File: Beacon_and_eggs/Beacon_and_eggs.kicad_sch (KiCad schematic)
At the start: 34 parts, among them SW1 Boot, SW2 Reset, U1 SA818V, U2 STM32F411CEUx, U3 ADXL343, U4 MIC2877-5.0YFT-TR, U5 LM3940ISX-3.3/NOPB, Y1 25MHz 18pF, Y2 32.768kHz 12.5pF

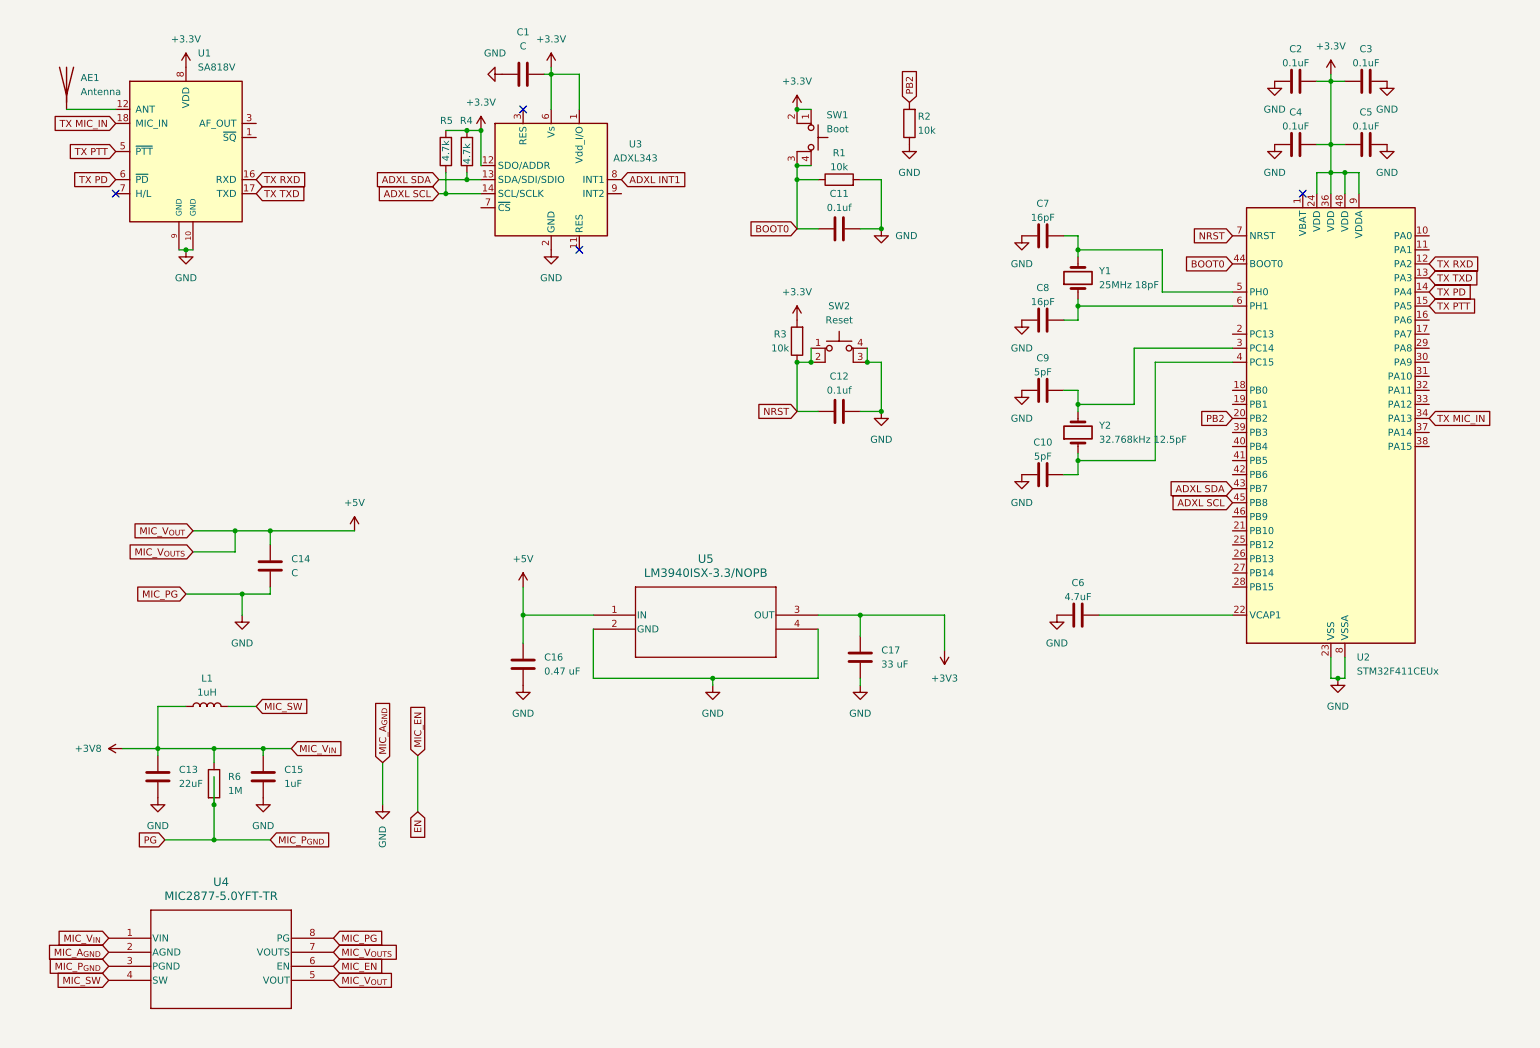
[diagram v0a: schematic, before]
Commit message: Reformatted Schematic Layout
cool beans
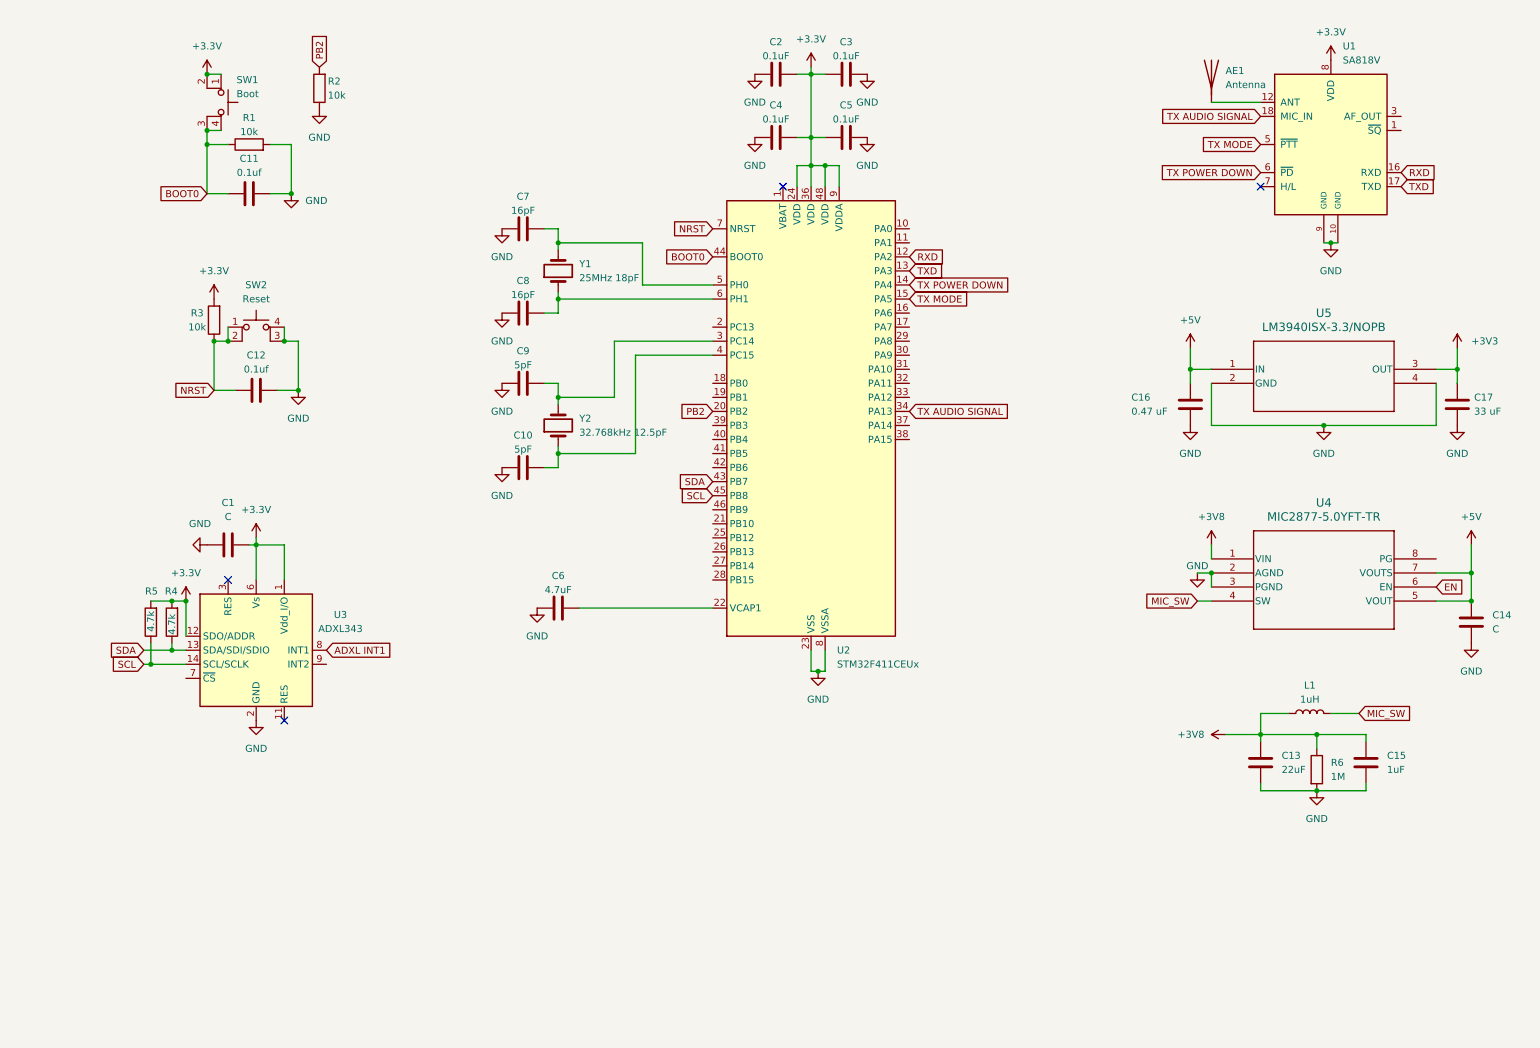
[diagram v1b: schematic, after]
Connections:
- net MIC_P_{GND} is gone; now on net GND: R6.2, U4.3 (PGND)
- net +5V: now also C14.2; no longer C14.1
- net GND: now also C14.1; no longer C14.2, U4.8 (PG)
- net ADXL SCL renamed SCL
- net ADXL SDA renamed SDA
- net TX MIC_IN renamed TX AUDIO SIGNAL
- net TX PD renamed TX POWER DOWN
- net TX PTT renamed TX MODE
- net TX RXD renamed RXD
- net TX TXD renamed TXD
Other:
- moved on the sheet: AE1, C1, C10, C11, C12, C13, C14, C15, C16, C17, C2, C3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

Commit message: Implemented new boost/buck converter
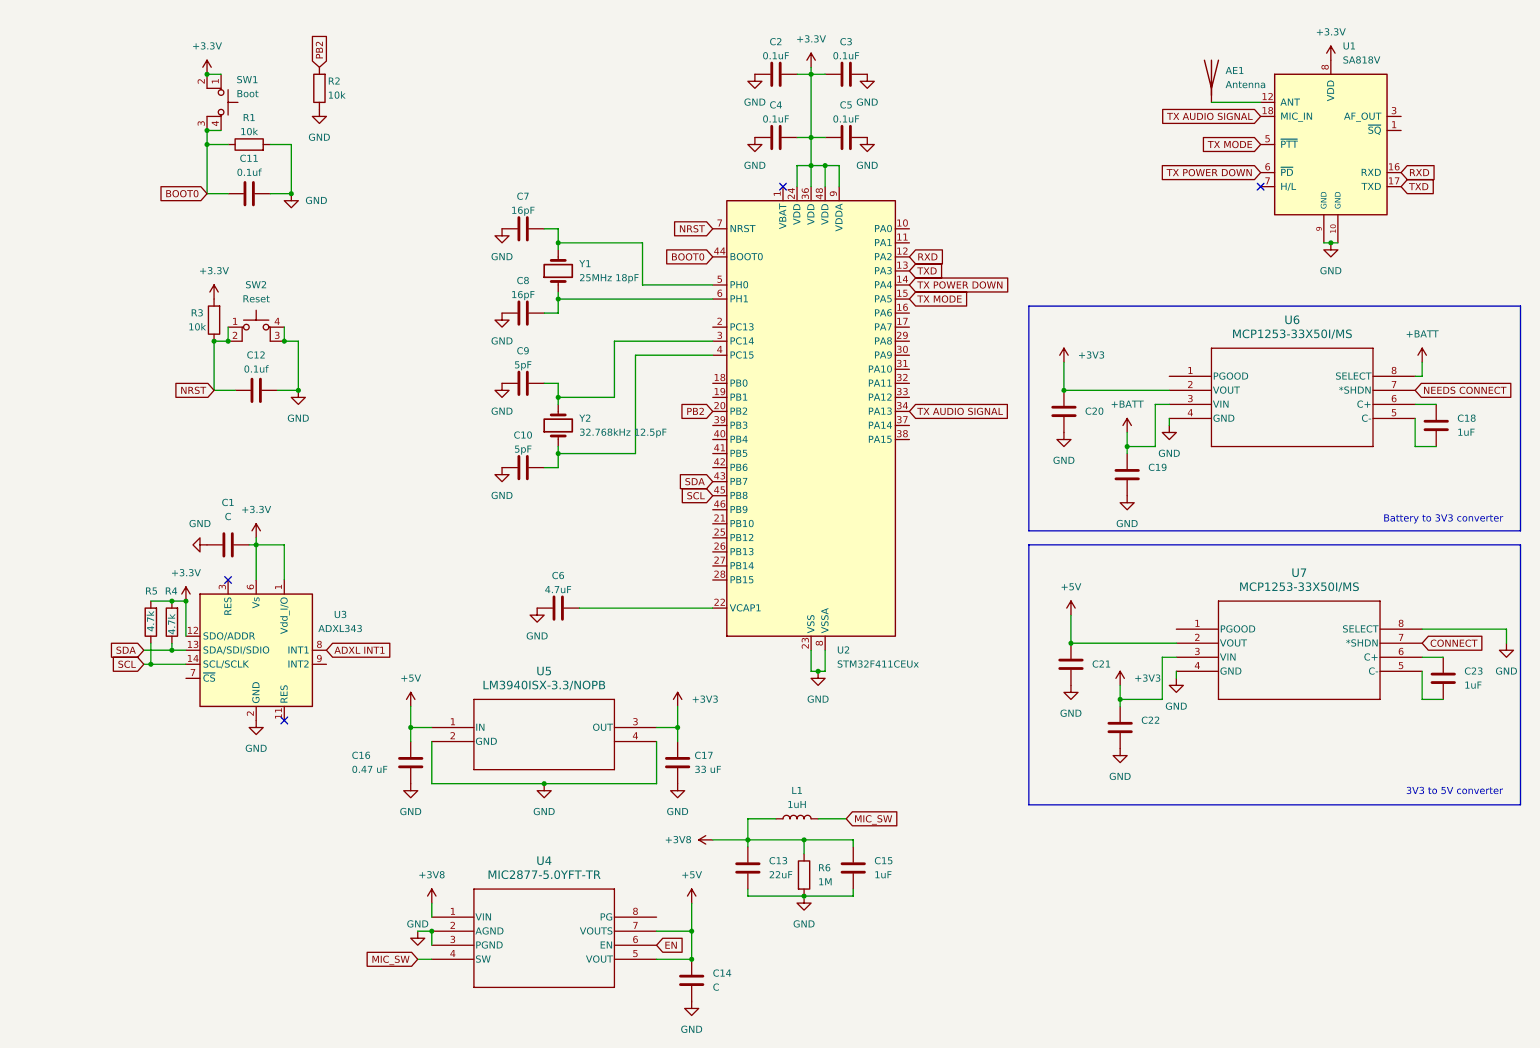
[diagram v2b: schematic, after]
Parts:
- added C18, C23: 1uF, Capacitor_SMD:C_1206_3216Metric, symbol Device:C
- added C19, C20, C21, C22: 10uF, Capacitor_SMD:C_1206_3216Metric, symbol Device:C
- added U6, U7: MCP1253-33X50I/MS, MSOP8_MC_MCH, symbol 2025_26-UVR-Beacon:MCP1253-33X50I_MS
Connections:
- net +3V3: now also C20.1, C22.1, U6.2 (VOUT), U7.3 (VIN)
- net +5V: now also C21.1, U7.2 (VOUT)
- net GND: now also C19.2, C20.2, C21.2, C22.2, U6.4 (GND), U7.4 (GND), U7.8 (SELECT)
- new net: C23.2, U7.5 (C-)
- new net: C23.1, U7.6 (C+)
- new net: C18.1, U6.6 (C+)
- new net: C18.2, U6.5 (C-)
- new net +BATT: C19.1, U6.3 (VIN), U6.8 (SELECT)
- new net CONNECT: U7.7 (*SHDN)
- new net NEEDS CONNECT: U6.7 (*SHDN)
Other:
- note added: "3V3 to 5V converter"
- note added: "Battery to 3V3 converter"
- moved on the sheet: C13, C14, C15, C16, C17, L1, R6, U4, U5

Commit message: Update Beacon_and_eggs.kicad_sch
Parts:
- removed C13: 22uF, Capacitor_SMD:C_1206_3216Metric, symbol Device:C
- removed C14: C, Capacitor_SMD:C_1206_3216Metric, symbol Device:C
- removed C15: 1uF, Capacitor_SMD:C_1206_3216Metric, symbol Device:C
- removed C16: 0.47 uF, symbol Device:C
- removed C17: 33 uF, symbol Device:C
- removed L1: 1uH, 2025_26-UVR-Beacon:INDM5752X300N, symbol Device:L
- removed R6: 1M, Resistor_SMD:R_1206_3216Metric, symbol Device:R
- removed U4: MIC2877-5.0YFT-TR, 2025_26-UVR-Beacon:MIC2877, symbol 2025_26-UVR-Beacon:MIC2877-5.0YFT-TR
- removed U5: LM3940ISX-3.3/NOPB, 2025_26-UVR-Beacon:LM3940, symbol 2025_26-UVR-Beacon:LM3940ISX-3.3_NOPB

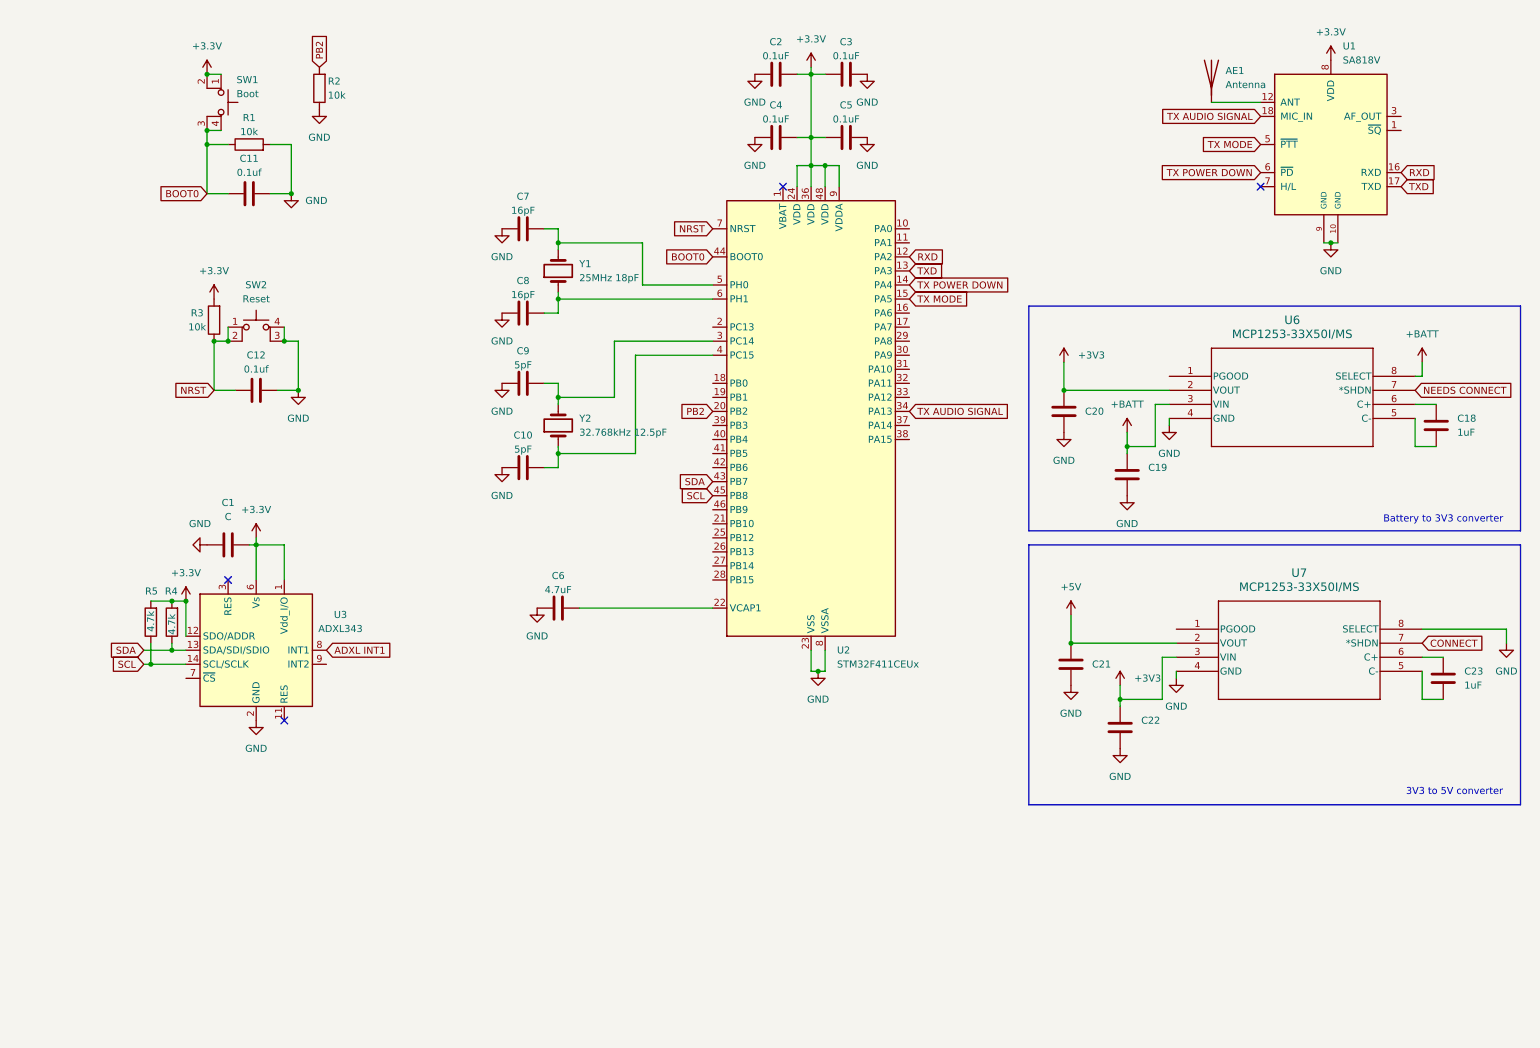
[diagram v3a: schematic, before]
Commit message: Buzzer, USB, and Documentation
Added the buzzer and USB c circuits, alongside adding boxes with labels to the remaining parts of the circuit
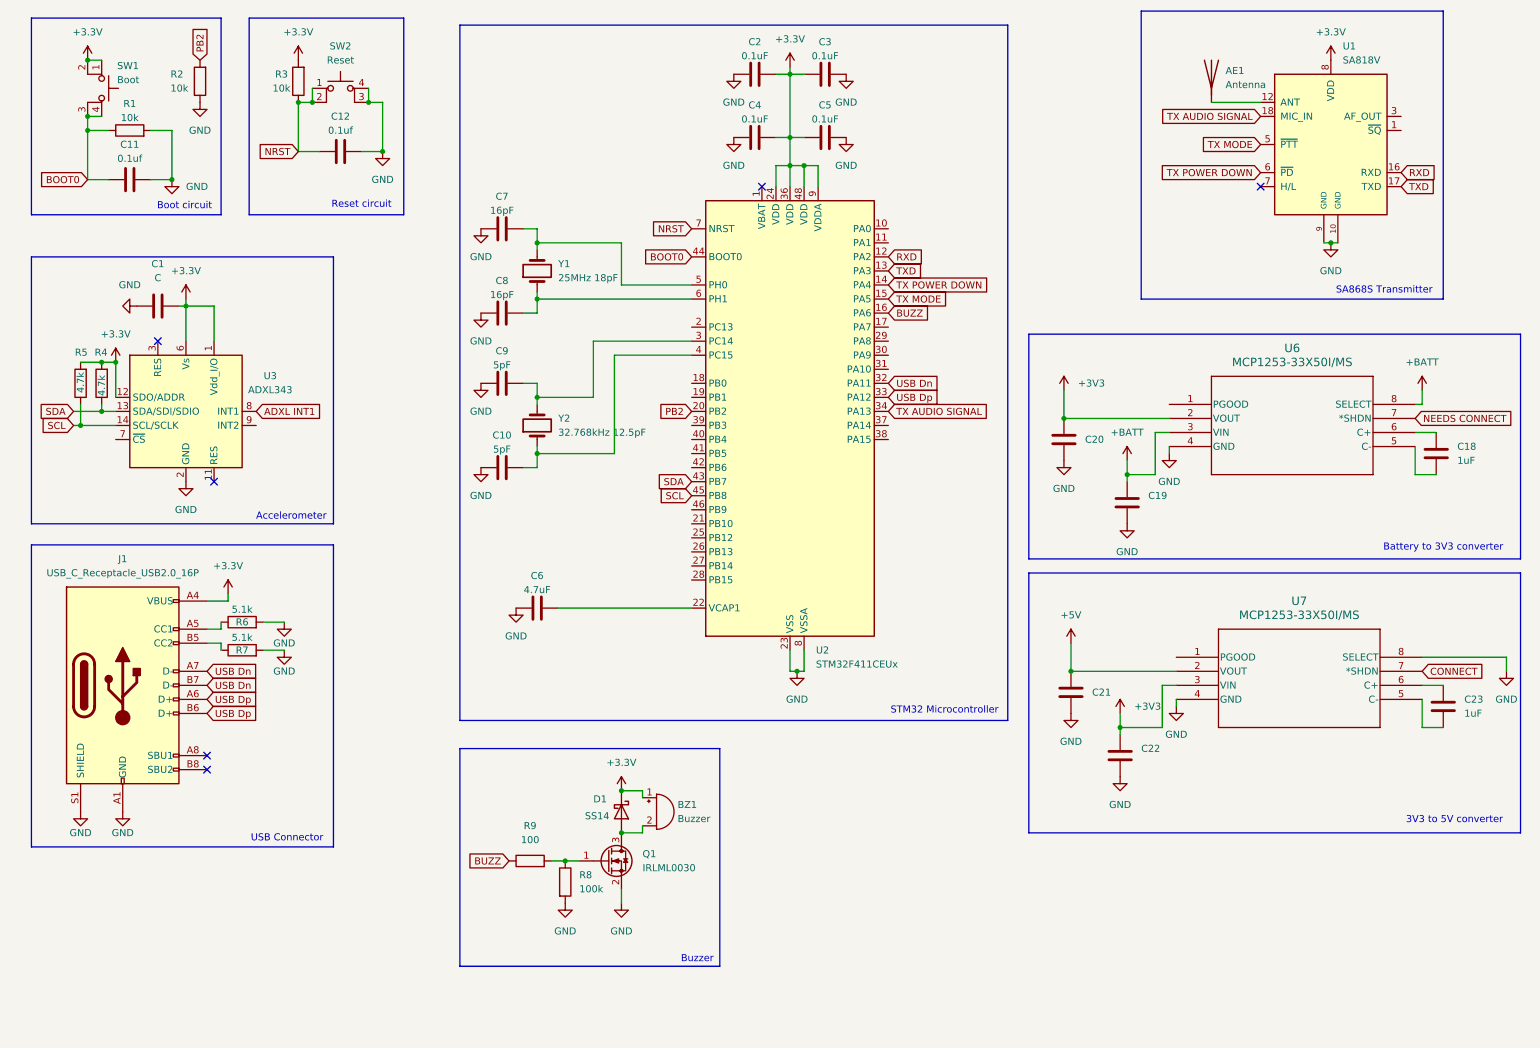
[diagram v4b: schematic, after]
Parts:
- added BZ1: Buzzer, symbol Device:Buzzer
- added D1: SS14, Diode_SMD:D_SMA, symbol Diode:SS14
- added J1: USB_C_Receptacle_USB2.0_16P, symbol Connector:USB_C_Receptacle_USB2.0_16P
- added Q1: IRLML0030, Package_TO_SOT_SMD:SOT-23, symbol Transistor_FET:IRLML0030
- added R6, R7: 5.1k, symbol Device:R
- added R8: 100k, symbol Device:R
- added R9: 100, symbol Device:R
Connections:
- net +3.3V: now also BZ1.1 (+), D1.1 (K), J1.A4 (VBUS), J1.A9 (VBUS), J1.B4 (VBUS), J1.B9 (VBUS)
- net GND: now also J1.A1 (GND), J1.A12 (GND), J1.B1 (GND), J1.B12 (GND), J1.S1 (SHIELD), Q1.2 (S), R6.2, R7.2, R8.2
- net BUZZ: now reaches U2.16 (PA6)
- net BUZZ: now also R9.1
- net USB Dn: now reaches U2.32 (PA11)
- net USB Dn: now also J1.A7 (D-), J1.B7 (D-)
- net USB Dp: now reaches U2.33 (PA12)
- net USB Dp: now also J1.A6 (D+), J1.B6 (D+)
- new net: J1.A5 (CC1), R6.1
- new net: J1.B5 (CC2), R7.1
- new net: Q1.1 (G), R8.1, R9.2
- new net: BZ1.2 (-), D1.2 (A), Q1.3 (D)
- no-connect marks 4 -> 6
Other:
- note added: "Accelerometer"
- note added: "Boot circuit"
- note added: "Buzzer"
- note added: "Reset circuit"
- note added: "SA868S Transmitter"
- note added: "STM32 Microcontroller"
- note added: "USB Connector"
- moved on the sheet: C1, C10, C11, C12, C18, C19, C2, C20, C21, C22, C23, C3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
